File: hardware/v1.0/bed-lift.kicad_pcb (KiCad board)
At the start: 4 copper layers, 195 x 45 mm, 143 parts, among them J1 SM04B-SRSS-TB, J10 Molex Mini Fit Jr 39-30-1060, J11 S4B-XH-A, J12 S4B-XH-A, J13 S4B-XH-A, J14 S4B-XH-A, J2 S2P-VH, J3 SM04B-SRSS-TB, J4 S3B-XH-A, J5 S6B-XH-A, J6 Conn_ST_STDC14, J7 S6B-XH-A, J8 Conn_02x08_Odd_Even, J9 Molex Mini Fit Jr 39-30-1060, Q1 MMBT3904, U1 LP2985-33DBVR, U10 DRV8434SPWPR, U2 LP2985-5.0DBVR, U3 ISO1640, U4 STM32C051C8T6, U5 DRV8874PWPR, U6 DRV8874PWPR, U7 DRV8434SPWPR, U8 DRV8434SPWPR, U9 DRV8434SPWPR

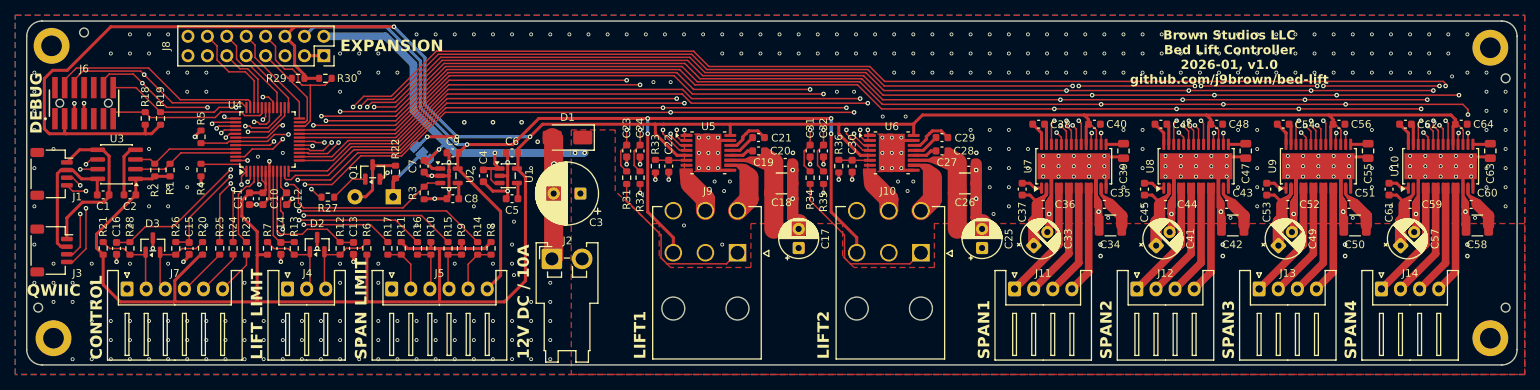
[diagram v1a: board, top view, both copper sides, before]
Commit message: Improve power distribution.
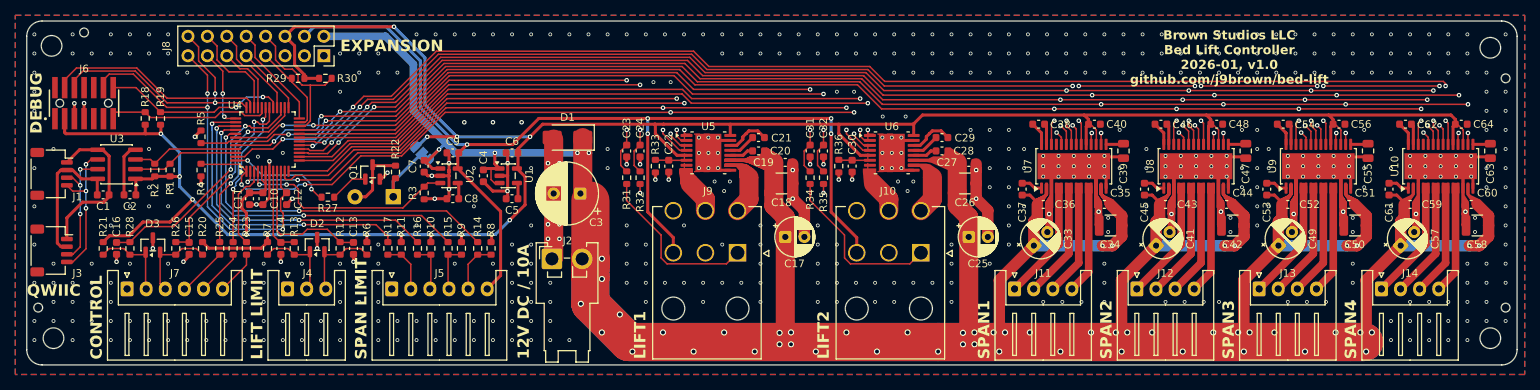
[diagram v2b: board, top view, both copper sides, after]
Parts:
- MP1, MP2, MP3, MP4: value MountingHole_2.7mm_M2.5_DIN965_Pad -> MountingHole_2.7mm_M2.5; footprint MountingHole:MountingHole_2.7mm_M2.5_DIN965_Pad -> MountingHole:MountingHole_2.7mm_M2.5
- moved C43 8.00 mm to (178.0, 79.2), turned to 0 degrees
- moved C44 8.00 mm to (186.0, 79.2), turned to 180 degrees
- moved C17 2.28 mm to (128.2, 83.5), turned to 0 degrees
- moved C25 2.28 mm to (152.2, 83.5), turned to 0 degrees
- turned R20 to -90 degrees
- turned R21 to -90 degrees
- turned R6 to -90 degrees
- turned R7 to -90 degrees
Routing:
- net +12V: track 156.7 -> 510.8 mm, vias 12 -> 56
- net +3.3V: track 440.7 -> 356.2 mm, vias 4 -> 15
- net /SWCLK/BOOT0: track 32.1 -> 35.1 mm, vias 1 -> 2
- net GND: track 153.8 -> 153.7 mm, vias 464 -> 560
- net /EXP_PA15: vias 1 -> 2
- removed copper zone on F.Cu, net +12V

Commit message: Further refinement, ready for fabrication.
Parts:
- added C10: 1u, Capacitor_SMD:C_0603_1608Metric, F.Cu at (90.2, 86.0)
- added C23: 100n, Capacitor_SMD:C_0402_1005Metric, F.Cu at (112.0, 71.2)
- added C26: 1u, Capacitor_SMD:C_0603_1608Metric, F.Cu at (112.2, 76.8)
- added C33: 100n, Capacitor_SMD:C_0402_1005Metric, F.Cu at (136.0, 71.2)
- added C36: 1u, Capacitor_SMD:C_0603_1608Metric, F.Cu at (136.2, 76.8)
- added D4: KT-0603R, LED_SMD:LED_0603_1608Metric, F.Cu at (61.5, 63.0)
- added D5: PESD3V3L5UY, Package_TO_SOT_SMD:SOT-363_SC-70-6, F.Cu at (46.0, 66.0)
- added D6: PESD5V0S2UAT, Package_TO_SOT_SMD:SOT-23, F.Cu at (108.5, 76.8)
- added D7: PESD5V0S2UAT, Package_TO_SOT_SMD:SOT-23, F.Cu at (132.5, 76.8)
- added J8: BM04B-SRSS-TB, Connector_JST:JST_SH_BM04B-SRSS-TB_1x04-1MP_P1.00mm_Vertical, F.Cu at (41.8, 57.8)
- added R29: 2.2K, Resistor_SMD:R_0402_1005Metric, F.Cu at (62.0, 64.5)
- C1, C13, C14, C2, C5, C8: footprint Capacitor_SMD:C_0603_1608Metric -> Capacitor_SMD:C_0402_1005Metric
- C15: renamed from C12; footprint Capacitor_SMD:C_0603_1608Metric -> Capacitor_SMD:C_0402_1005Metric
- C16: renamed from C15; footprint Capacitor_SMD:C_0603_1608Metric -> Capacitor_SMD:C_0402_1005Metric
- C17: renamed from C16; footprint Capacitor_SMD:C_0603_1608Metric -> Capacitor_SMD:C_0402_1005Metric
- C24: renamed from C22; footprint Capacitor_SMD:C_0603_1608Metric -> Capacitor_SMD:C_0402_1005Metric
- C25: renamed from C23; footprint Capacitor_SMD:C_0603_1608Metric -> Capacitor_SMD:C_0402_1005Metric
- C27: renamed from C24; footprint Capacitor_SMD:C_0603_1608Metric -> Capacitor_SMD:C_0402_1005Metric
- C34: renamed from C30; footprint Capacitor_SMD:C_0603_1608Metric -> Capacitor_SMD:C_0402_1005Metric
- C35: renamed from C31; footprint Capacitor_SMD:C_0603_1608Metric -> Capacitor_SMD:C_0402_1005Metric
- C37: renamed from C32; footprint Capacitor_SMD:C_0603_1608Metric -> Capacitor_SMD:C_0402_1005Metric
- R1, R10, R11, R12, R13, R14, R15, R16, R17, R2, R20, R21, R23, R24, R25, R26, R27, R28, R3, R4, R5, R6, R7, R8, R9: footprint Resistor_SMD:R_0603_1608Metric -> Resistor_SMD:R_0402_1005Metric
- R18: renamed from R29; footprint Resistor_SMD:R_0603_1608Metric -> Resistor_SMD:R_0402_1005Metric
- R19: renamed from R30; footprint Resistor_SMD:R_0603_1608Metric -> Resistor_SMD:R_0402_1005Metric
- R22: value 1K -> 3.3K
- R30: renamed from R18; footprint Resistor_SMD:R_0603_1608Metric -> Resistor_SMD:R_0402_1005Metric
- R31: renamed from R19; footprint Resistor_SMD:R_0603_1608Metric -> Resistor_SMD:R_0402_1005Metric
- R32: renamed from R31; footprint Resistor_SMD:R_0603_1608Metric -> Resistor_SMD:R_0402_1005Metric
- R33: renamed from R32; footprint Resistor_SMD:R_0603_1608Metric -> Resistor_SMD:R_0402_1005Metric
- R34: renamed from R33; footprint Resistor_SMD:R_0603_1608Metric -> Resistor_SMD:R_0402_1005Metric
- R35: renamed from R34; footprint Resistor_SMD:R_0603_1608Metric -> Resistor_SMD:R_0402_1005Metric
- R36: renamed from R35; footprint Resistor_SMD:R_0603_1608Metric -> Resistor_SMD:R_0402_1005Metric
- R37: renamed from R36; footprint Resistor_SMD:R_0603_1608Metric -> Resistor_SMD:R_0402_1005Metric
- U2: value LP2985-5.0DBVR -> LP2985-50DBVR
- moved R19 18.0 mm to (50.6, 58.2), turned to 90 degrees
- moved R18 13.3 mm to (52.0, 58.2), turned to 90 degrees
- moved R6 5.34 mm to (68.2, 86.0)
- moved J6 5.00 mm to (72.9, 59.8)
- moved R31 4.78 mm to (43.2, 64.5)
- moved R21 4.61 mm to (43.5, 86.0)
- moved R20 3.64 mm to (48.5, 86.0)
- moved R17 3.16 mm to (79.2, 86.0)
- moved R7 2.93 mm to (63.2, 86.0)
- moved R11 2.69 mm to (80.5, 86.0)
- moved R32 2.26 mm to (107.8, 73.5)
- moved R35 2.26 mm to (131.8, 73.5)
- moved R33 2.25 mm to (109.2, 73.5)
- moved R36 2.25 mm to (133.2, 73.5)
- moved R13 2.24 mm to (62.0, 86.0)
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- renumbered C10 to C11, C11 to C12, C17 to C18, C18 to C19, C19 to C20, C20 to C21, C21 to C22, C25 to C28, C26 to C29, C27 to C30, C28 to C31, C29 to C32, C33 to C38, C34 to C39, C35 to C40, C36 to C41, C37 to C42, C38 to C43, C39 to C44, C40 to C45, C41 to C46, C42 to C47, C43 to C48, C44 to C49, C45 to C50, C46 to C51, C47 to C52, C48 to C53, C49 to C54, C50 to C55, C51 to C56, C52 to C57, C53 to C58, C54 to C59, C55 to C60, C56 to C61, C57 to C62, C58 to C63, C59 to C64, C60 to C65, C61 to C66, C62 to C67, C63 to C68, C64 to C69, J9 to J10, J10 to J11, J11 to J12, J12 to J13, J13 to J14, J14 to J15, J8 to J6, J6 to J9
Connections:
- net /LED_B renamed /LED_STATUS_B
- net /LED_G renamed /LED_STATUS_G
- net /LED_R renamed /LED_STATUS_R
- J1 pad MP: unconnected-(J1-MountPin-PadMP)_1 -> /BUS_GND
- J3 pad MP: unconnected-(J3-MountPin-PadMP) -> /BUS_GND
- J6 pad 12: /EXP_PA8 -> /EXP_PA12
- J6 pad 14: /EXP_PA12 -> unconnected-(J6-Pin_14-Pad14)
- U4 pad 28: /EXP_PA8 -> /~{LED_POWER}
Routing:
- net /INT_I2C_SDA: track 12.1 -> 34.3 mm, vias 0 -> 1
- net +3.3V: track 356.2 -> 377.9 mm, vias 15 -> 18
- net /INT_I2C_SCL: track 19.6 -> 38.2 mm, vias 0 -> 1
- net /EXP_PA8: track 12.6 -> 0.00 mm
- net GND: track 153.7 -> 158.4 mm, vias 560 -> 765
- net /~{SPAN1_LIMIT_A}: track 40.1 -> 44.6 mm
- net Net-(J7-Pin_3): track 11.2 -> 7.23 mm
- net /~{SPAN1_LIMIT_B}: track 42.3 -> 46.3 mm
- net +5V: track 141.0 -> 137.1 mm
- net Net-(J7-Pin_2): track 10.7 -> 6.98 mm
- net Net-(J10-Pin_1): track 22.5 -> 25.7 mm
- net Net-(J11-Pin_1): track 22.5 -> 25.7 mm
- net /EXP_PA12: track 13.1 -> 9.88 mm
- net Net-(J4-Pin_3): track 10.8 -> 7.99 mm
- net /~{SPAN2_LIMIT_A}: track 43.1 -> 45.8 mm
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- added copper zone on F.Cu, net /BUS_GND
- added copper zone on In1.Cu, net /BUS_GND
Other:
- board text added: "BT0 (NC) PA12 PB12 SCL 3V3 5V 12V"
- board text added: "EXT I2C"
- board text added: "INT I2C"
- board text added: "POWER"
- board text removed: "BT0 PA12 PA8 PB12 SCL 3V3 5V 12V"
- board text removed: "QWIIC"
